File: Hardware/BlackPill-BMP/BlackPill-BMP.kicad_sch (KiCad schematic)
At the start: 39 parts, among them J1 JTAG, J2 VCC, J3 GND, J4 SWO, J5 GDB_COMM, J6 TVCC, J7 LogicAna, J8 Conn_01x10, J9 Conn_01x11, U1 BlueAndBlackPill, U2 AD8531ARTZ, U3 SRV05-4, U4 TXS0108EPW, U5 SRV05-4

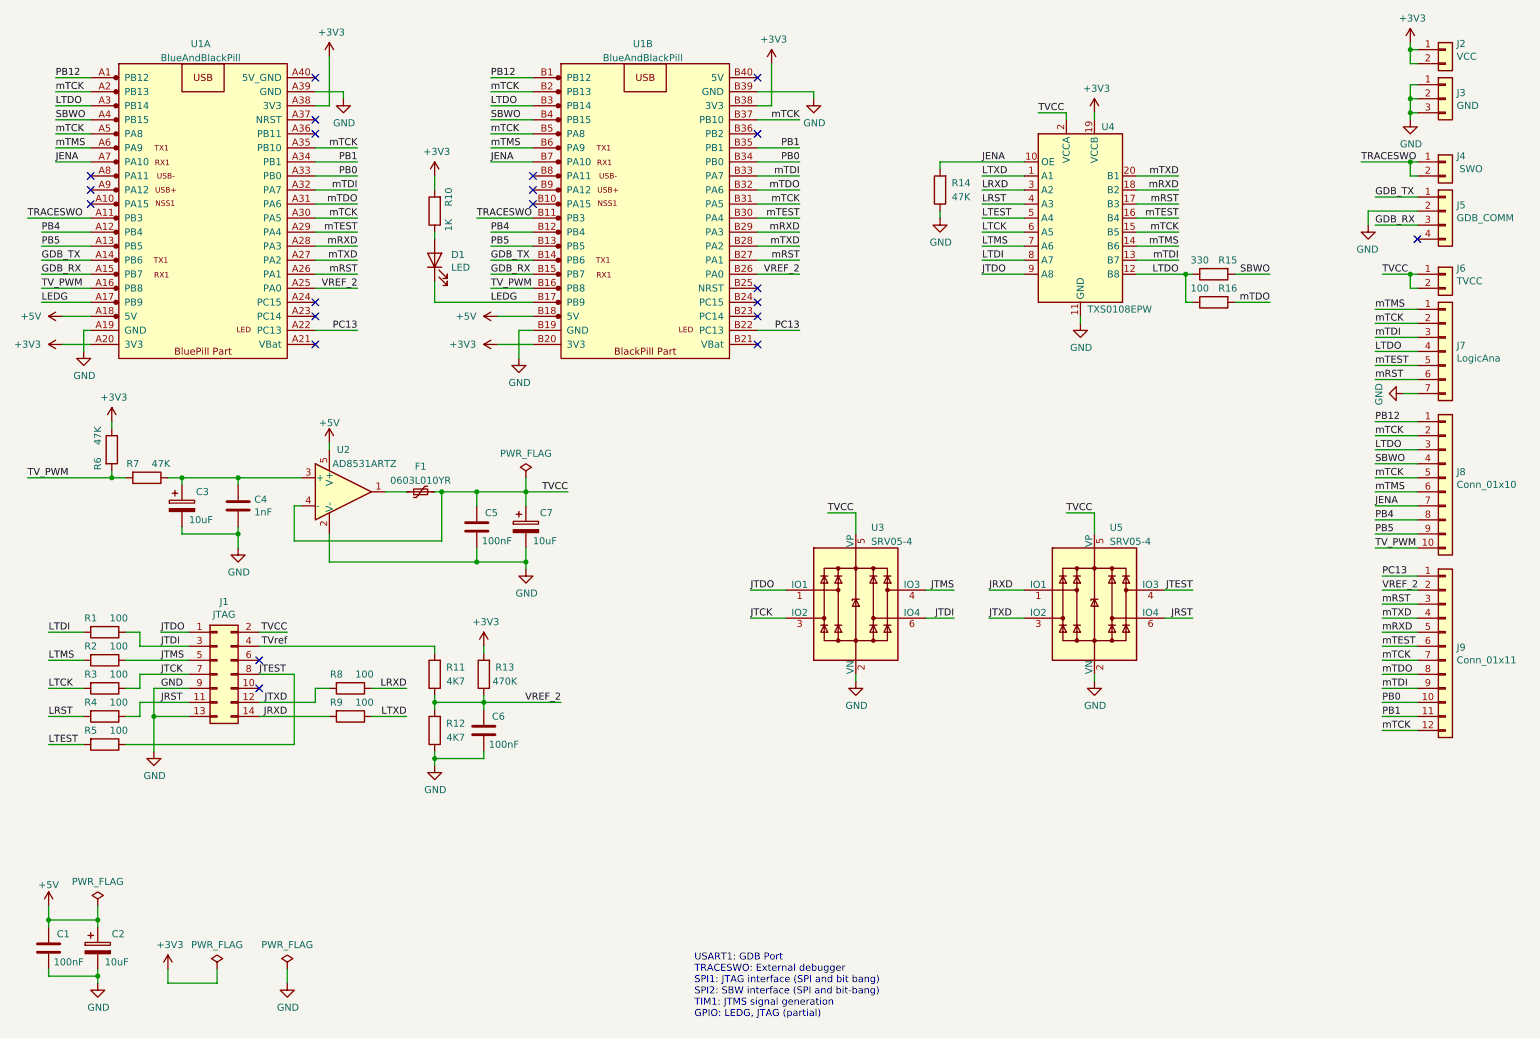
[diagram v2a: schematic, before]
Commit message: Variable voltage level for the L432KC board. Minor fixes on the Blue+Blackpill board.
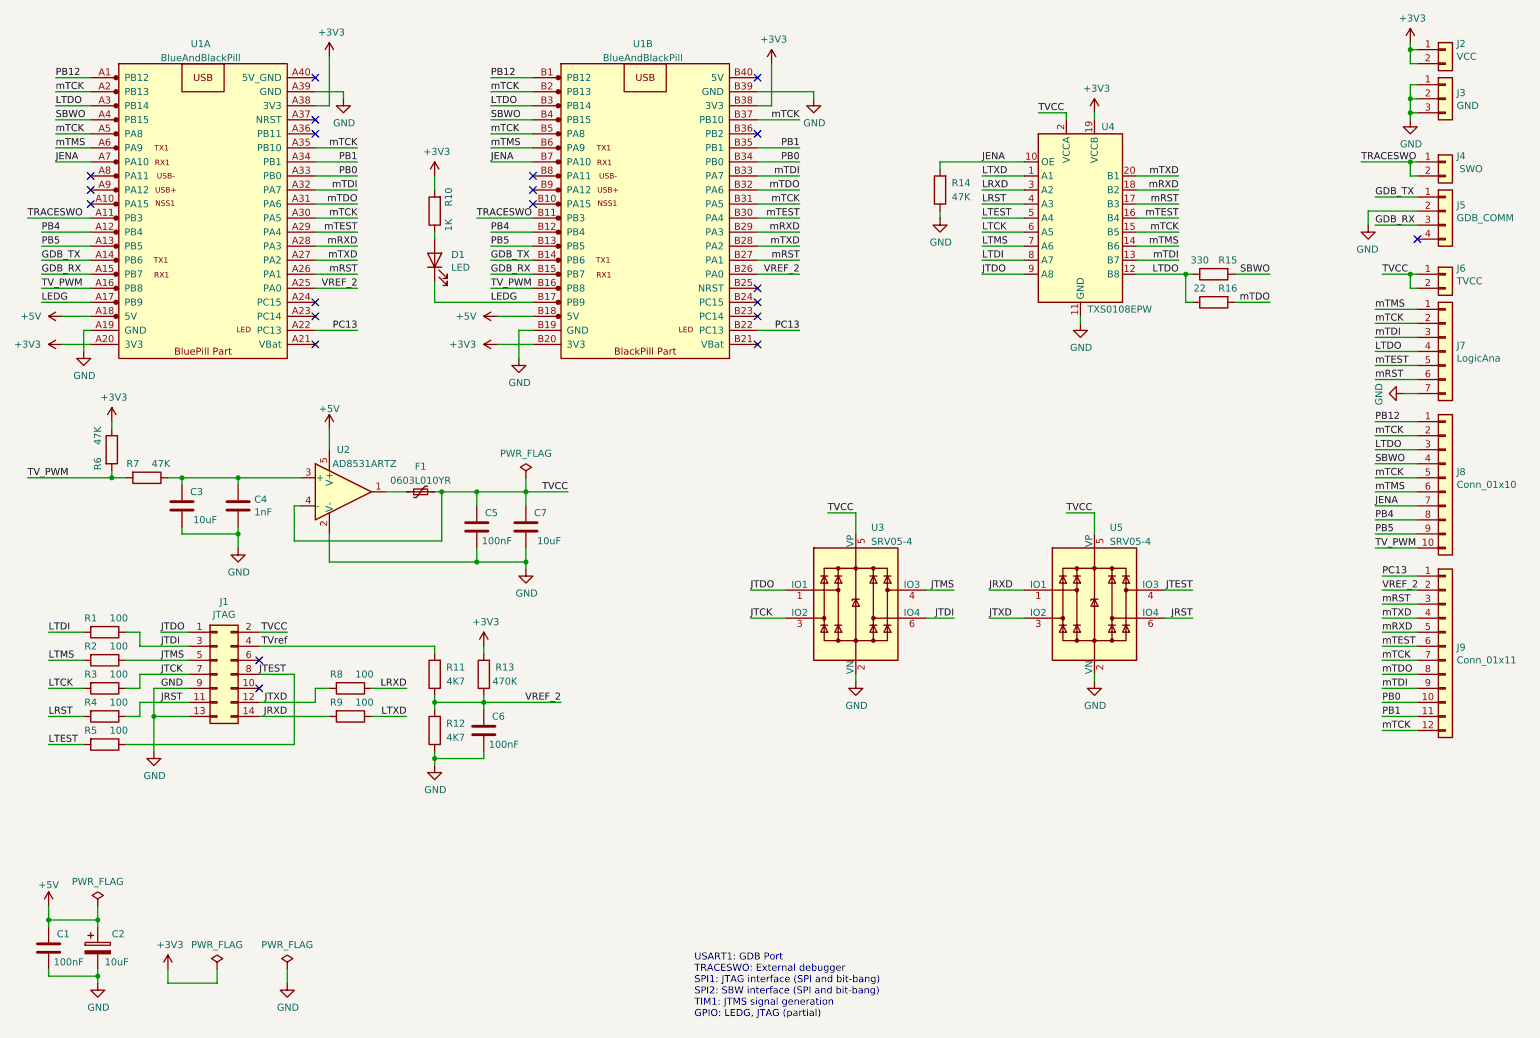
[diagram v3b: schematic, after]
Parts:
- removed C3, C7: 10uF, Capacitor_SMD:C_0603_1608Metric_Pad1.08x0.95mm_HandSolder, symbol Device:C_Polarized
- added C3, C7: 10uF, Capacitor_SMD:C_0603_1608Metric_Pad1.08x0.95mm_HandSolder, symbol Device:C
- R16: value 100 -> 22
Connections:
- net GND: now also C3.1, C7.1
- net TVCC: now also C7.2
- net at C4.1, R7.1, U2.3 (+): now also C3.2
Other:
- note added: "USART1: GDB Port TRACESWO: External debugger SPI1: JTAG interface (SPI and bit-bang) SPI2: SBW interface (SPI and bit-bang) TIM1: JTMS signal generation GPIO: LEDG, JTAG (partial)"
- note removed: "USART1: GDB Port TRACESWO: External debugger SPI1: JTAG interface (SPI and bit bang) SPI2: SBW interface (SPI and bit-bang) TIM1: JTMS signal generation GPIO: LEDG, JTAG (partial)"
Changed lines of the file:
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@@
   (title_block
     (title "MSPBMP Development Protoboard")
-    (date "2022-01-09")
-    (rev "3")
+    (date "2022-08-02")
+    (rev "1")
     (company "Mathias Gruber")
-    (comment 1 "With optional TRACE SWO using FT232RL")
+    (comment 1 "BluePill and BlackPill option")
   )
   (junction (at 265.43 40.64) (diameter 0) (color 0 0 0 0)
@@
     (stroke (width 0) (type default) (color 0 0 0 0))
   )
-  (wire (pts (xy 69.85 91.44) (xy 69.85 92.71))
+  (wire (pts (xy 69.85 88.9) (xy 69.85 92.71))
     (stroke (width 0) (type default) (color 0 0 0 0))
   )
@@
     (stroke (width 0) (type default) (color 0 0 0 0))
   )
-  (text "USART1: GDB Port\nTRACESWO: External debugger\nSPI1: JTAG interface (SPI and bit bang)\nSPI2: SBW interface (SPI and bit-bang)\nTIM1: JTMS signal generation\nGPIO: LEDG, JTAG (partial)"
+  (text "USART1: GDB Port\nTRACESWO: External debugger\nSPI1: JTAG interface (SPI and bit-bang)\nSPI2: SBW interface (SPI and bit-bang)\nTIM1: JTMS signal generation\nGPIO: LEDG, JTAG (partial)"
     (at 135.89 195.58 0)
     (effects (font (size 1.27 1.27)) (justify left bottom))
@@
     (in_bom yes) (on_board yes)
     (property "Reference" "R16" (id 0) (at 232.41 63.5 90))
-    (property "Value" "100" (id 1) (at 227.33 63.5 90))
+    (property "Value" "22" (id 1) (at 227.33 63.5 90))
     (property "Footprint" "Resistor_SMD:R_0603_1608Metric_Pad0.98x0.95mm_HandSolder" (id 2) (at 229.87 64.262 90)
       (effects (font (size 1.27 1.27)) hide)
@@
     (pin "1")
   )
-  (symbol (lib_id "power:+5V") (at 69.85 91.44 0) (unit 1)
+  (symbol (lib_id "power:+5V") (at 69.85 88.9 0) (unit 1)
     (in_bom yes) (on_board yes) (fields_autoplaced)
-    (property "Reference" "#PWR012" (id 0) (at 69.85 95.25 0)
-      (effects (font (size 1.27 1.27)) hide)
-    )
-    (property "Value" "+5V" (id 1) (at 69.85 87.8642 0))
-    (property "Footprint" "" (id 2) (at 69.85 91.44 0)
-      (effects (font (size 1.27 1.27)) hide)
-    )
-    (property "Datasheet" "" (id 3) (at 69.85 91.44 0)
+    (property "Reference" "#PWR012" (id 0) (at 69.85 92.71 0)
+      (effects (font (size 1.27 1.27)) hide)
+    )
+    (property "Value" "+5V" (id 1) (at 69.85 85.3242 0))
+    (property "Footprint" "" (id 2) (at 69.85 88.9 0)
+      (effects (font (size 1.27 1.27)) hide)
+    )
+    (property "Datasheet" "" (id 3) (at 69.85 88.9 0)
       (effects (font (size 1.27 1.27)) hide)
     )
@@
     (pin "1")
   )
-  (symbol (lib_id "Device:C_Polarized") (at 43.18 102.87 0) (unit 1)
-    (in_bom yes) (on_board yes)
-    (property "Reference" "C3" (id 0) (at 45.72 100.33 0)
-      (effects (font (size 1.27 1.27)) (justify left))
-    )
-    (property "Value" "10uF" (id 1) (at 44.45 105.41 0)
-      (effects (font (size 1.27 1.27)) (justify left))
-    )
-    (property "Footprint" "Capacitor_SMD:C_0603_1608Metric_Pad1.08x0.95mm_HandSolder" (id 2) (at 44.1452 106.68 0)
-      (effects (font (size 1.27 1.27)) hide)
-    )
-    (property "Datasheet" "~" (id 3) (at 43.18 102.87 0)
-      (effects (font (size 1.27 1.27)) hide)
-    )
-    (pin "1")
-    (pin "2")
-  )
   (symbol (lib_id "Device:R") (at 229.87 60.96 90) (mirror x) (unit 1)
     (in_bom yes) (on_board yes)
@@
     )
     (pin "1")
-  )
-  (symbol (lib_id "Device:C_Polarized") (at 105.41 106.68 0) (unit 1)
-    (in_bom yes) (on_board yes)
-    (property "Reference" "C7" (id 0) (at 107.95 104.14 0)
-      (effects (font (size 1.27 1.27)) (justify left))
-    )
-    (property "Value" "10uF" (id 1) (at 106.68 109.22 0)
-      (effects (font (size 1.27 1.27)) (justify left))
-    )
-    (property "Footprint" "Capacitor_SMD:C_0603_1608Metric_Pad1.08x0.95mm_HandSolder" (id 2) (at 106.3752 110.49 0)
-      (effects (font (size 1.27 1.27)) hide)
-    )
-    (property "Datasheet" "~" (id 3) (at 105.41 106.68 0)
-      (effects (font (size 1.27 1.27)) hide)
-    )
-    (pin "1")
-    (pin "2")
   )
   (symbol (lib_id "power:GND") (at 53.34 110.49 0) (unit 1)
@@
     (pin "1")
   )
+  (symbol (lib_id "Device:C") (at 43.18 102.87 180) (unit 1)
+    (in_bom yes) (on_board yes)
+    (property "Reference" "C3" (id 0) (at 46.99 100.33 0)
+      (effects (font (size 1.27 1.27)) (justify left))
+    )
+    (property "Value" "10uF" (id 1) (at 49.53 105.41 0)
+      (effects (font (size 1.27 1.27)) (justify left))
+    )
+    (property "Footprint" "Capacitor_SMD:C_0603_1608Metric_Pad1.08x0.95mm_HandSolder" (id 2) (at 42.2148 99.06 0)
+      (effects (font (size 1.27 1.27)) hide)
+    )
+    (property "Datasheet" "~" (id 3) (at 43.18 102.87 0)
+      (effects (font (size 1.27 1.27)) hide)
+    )
+    (pin "1")
+    (pin "2")
+  )
   (symbol (lib_id "power:GND") (at 180.34 50.8 0) (unit 1)
     (in_bom yes) (on_board yes)
@@
     (pin "2")
   )
+  (symbol (lib_id "Device:C") (at 105.41 106.68 180) (unit 1)
+    (in_bom yes) (on_board yes)
+    (property "Reference" "C7" (id 0) (at 109.22 104.14 0)
+      (effects (font (size 1.27 1.27)) (justify left))
+    )
+    (property "Value" "10uF" (id 1) (at 111.76 109.22 0)
+      (effects (font (size 1.27 1.27)) (justify left))
+    )
+    (property "Footprint" "Capacitor_SMD:C_0603_1608Metric_Pad1.08x0.95mm_HandSolder" (id 2) (at 104.4448 102.87 0)
+      (effects (font (size 1.27 1.27)) hide)
+    )
+    (property "Datasheet" "~" (id 3) (at 105.41 106.68 0)
+      (effects (font (size 1.27 1.27)) hide)
+    )
+    (pin "1")
+    (pin "2")
+  )
   (sheet_instances
     (path "/" (page "1"))
@@
       (reference "C2") (unit 1) (value "10uF") (footprint "Capacitor_SMD:C_0603_1608Metric_Pad1.08x0.95mm_HandSolder")
     )
-    (path "/1f912d12-5f1e-4d3a-9386-b3a1556da17c"
+    (path "/c4412be8-8b32-48a7-ad31-c4f3b68b0aa7"
       (reference "C3") (unit 1) (value "10uF") (footprint "Capacitor_SMD:C_0603_1608Metric_Pad1.08x0.95mm_HandSolder")
     )
@@
       (reference "C6") (unit 1) (value "100nF") (footprint "Capacitor_SMD:C_0603_1608Metric_Pad1.08x0.95mm_HandSolder")
     )
-    (path "/a8310ad3-96c4-466c-b689-168bae9ce861"
+    (path "/f9b264ce-55ff-44ff-b37a-2e7f4a5cfb85"
       (reference "C7") (unit 1) (value "10uF") (footprint "Capacitor_SMD:C_0603_1608Metric_Pad1.08x0.95mm_HandSolder")
     )
@@
     )
     (path "/00000000-0000-0000-0000-0000619ec4b5"
-      (reference "R16") (unit 1) (value "100") (footprint "Resistor_SMD:R_0603_1608Metric_Pad0.98x0.95mm_HandSolder")
+      (reference "R16") (unit 1) (value "22") (footprint "Resistor_SMD:R_0603_1608Metric_Pad0.98x0.95mm_HandSolder")
     )
     (path "/b141b0b5-1c34-438f-8f5a-a2e1dda2ee83"

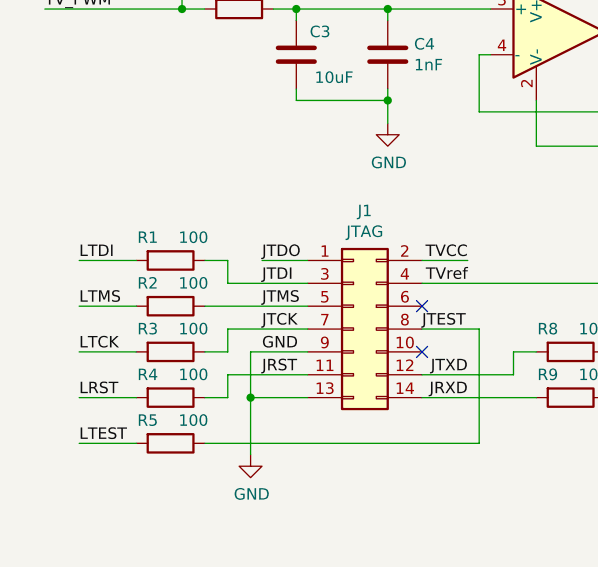
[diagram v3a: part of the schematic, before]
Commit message: Improved JTAG bus impedance for BlackPill. Various enhancements for Nucleo K432KC. Added SpiBiWire Adapter.
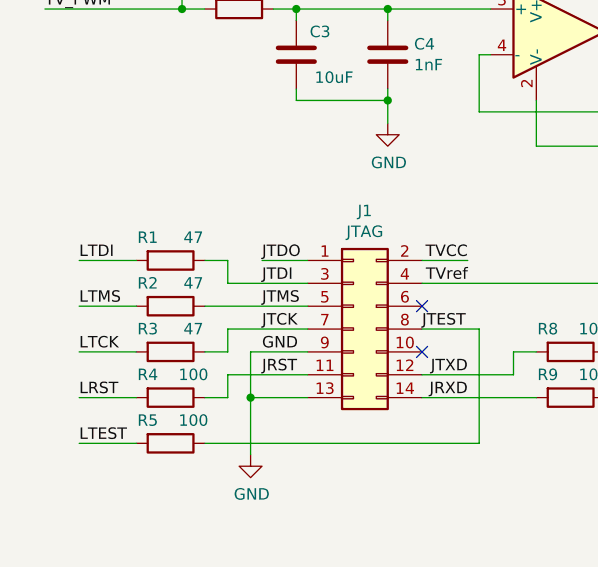
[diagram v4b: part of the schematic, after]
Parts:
- R1, R2, R3: value 100 -> 47
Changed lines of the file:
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@@
     (in_bom yes) (on_board yes)
     (property "Reference" "R2" (id 0) (at 26.67 128.27 90))
-    (property "Value" "100" (id 1) (at 31.75 128.27 90))
+    (property "Value" "47" (id 1) (at 31.75 128.27 90))
     (property "Footprint" "Resistor_SMD:R_0603_1608Metric_Pad0.98x0.95mm_HandSolder" (id 2) (at 29.21 129.032 90)
       (effects (font (size 1.27 1.27)) hide)
@@
     (in_bom yes) (on_board yes)
     (property "Reference" "R3" (id 0) (at 26.67 133.35 90))
-    (property "Value" "100" (id 1) (at 31.75 133.35 90))
+    (property "Value" "47" (id 1) (at 31.75 133.35 90))
     (property "Footprint" "Resistor_SMD:R_0603_1608Metric_Pad0.98x0.95mm_HandSolder" (id 2) (at 29.21 134.112 90)
       (effects (font (size 1.27 1.27)) hide)
@@
     (in_bom yes) (on_board yes)
     (property "Reference" "R1" (id 0) (at 26.67 123.19 90))
-    (property "Value" "100" (id 1) (at 31.75 123.19 90))
+    (property "Value" "47" (id 1) (at 31.75 123.19 90))
     (property "Footprint" "Resistor_SMD:R_0603_1608Metric_Pad0.98x0.95mm_HandSolder" (id 2) (at 29.21 123.952 90)
       (effects (font (size 1.27 1.27)) hide)
@@
     )
     (path "/00000000-0000-0000-0000-000061879062"
-      (reference "R1") (unit 1) (value "100") (footprint "Resistor_SMD:R_0603_1608Metric_Pad0.98x0.95mm_HandSolder")
+      (reference "R1") (unit 1) (value "47") (footprint "Resistor_SMD:R_0603_1608Metric_Pad0.98x0.95mm_HandSolder")
     )
     (path "/00000000-0000-0000-0000-000061874137"
-      (reference "R2") (unit 1) (value "100") (footprint "Resistor_SMD:R_0603_1608Metric_Pad0.98x0.95mm_HandSolder")
+      (reference "R2") (unit 1) (value "47") (footprint "Resistor_SMD:R_0603_1608Metric_Pad0.98x0.95mm_HandSolder")
     )
     (path "/00000000-0000-0000-0000-000061876db6"
-      (reference "R3") (unit 1) (value "100") (footprint "Resistor_SMD:R_0603_1608Metric_Pad0.98x0.95mm_HandSolder")
+      (reference "R3") (unit 1) (value "47") (footprint "Resistor_SMD:R_0603_1608Metric_Pad0.98x0.95mm_HandSolder")
     )
     (path "/00000000-0000-0000-0000-00006187bd4b"
